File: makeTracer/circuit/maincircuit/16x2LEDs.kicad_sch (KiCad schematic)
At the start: 39 parts, among them P1 FrontsidePort, U2 74HC595, U3 74HC595

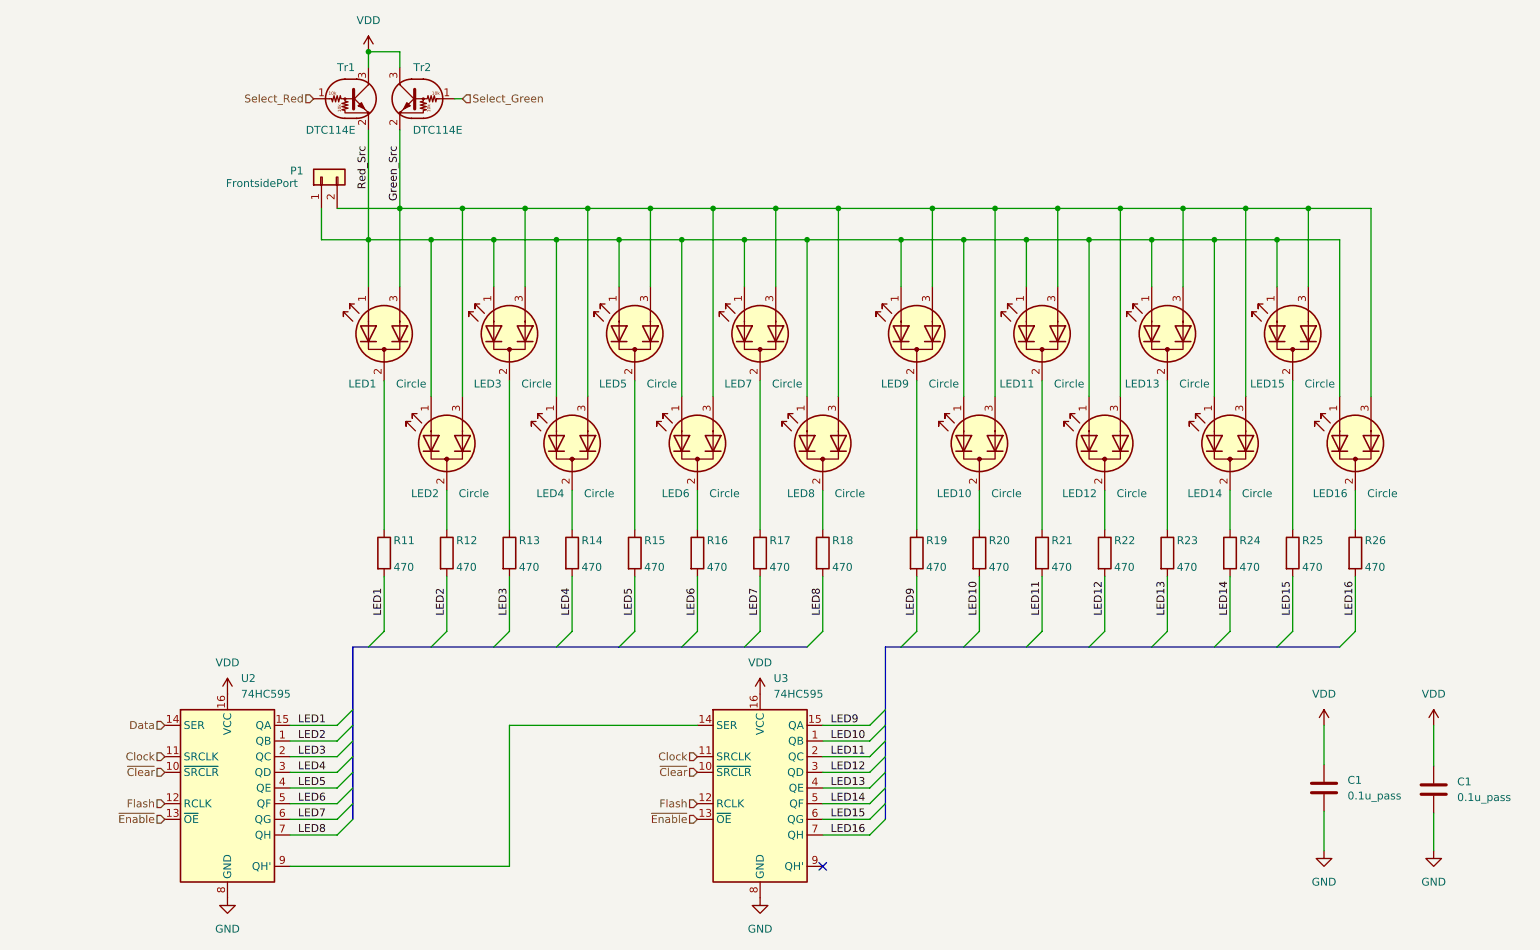
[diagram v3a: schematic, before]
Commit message: fix: .2mm to .4mm
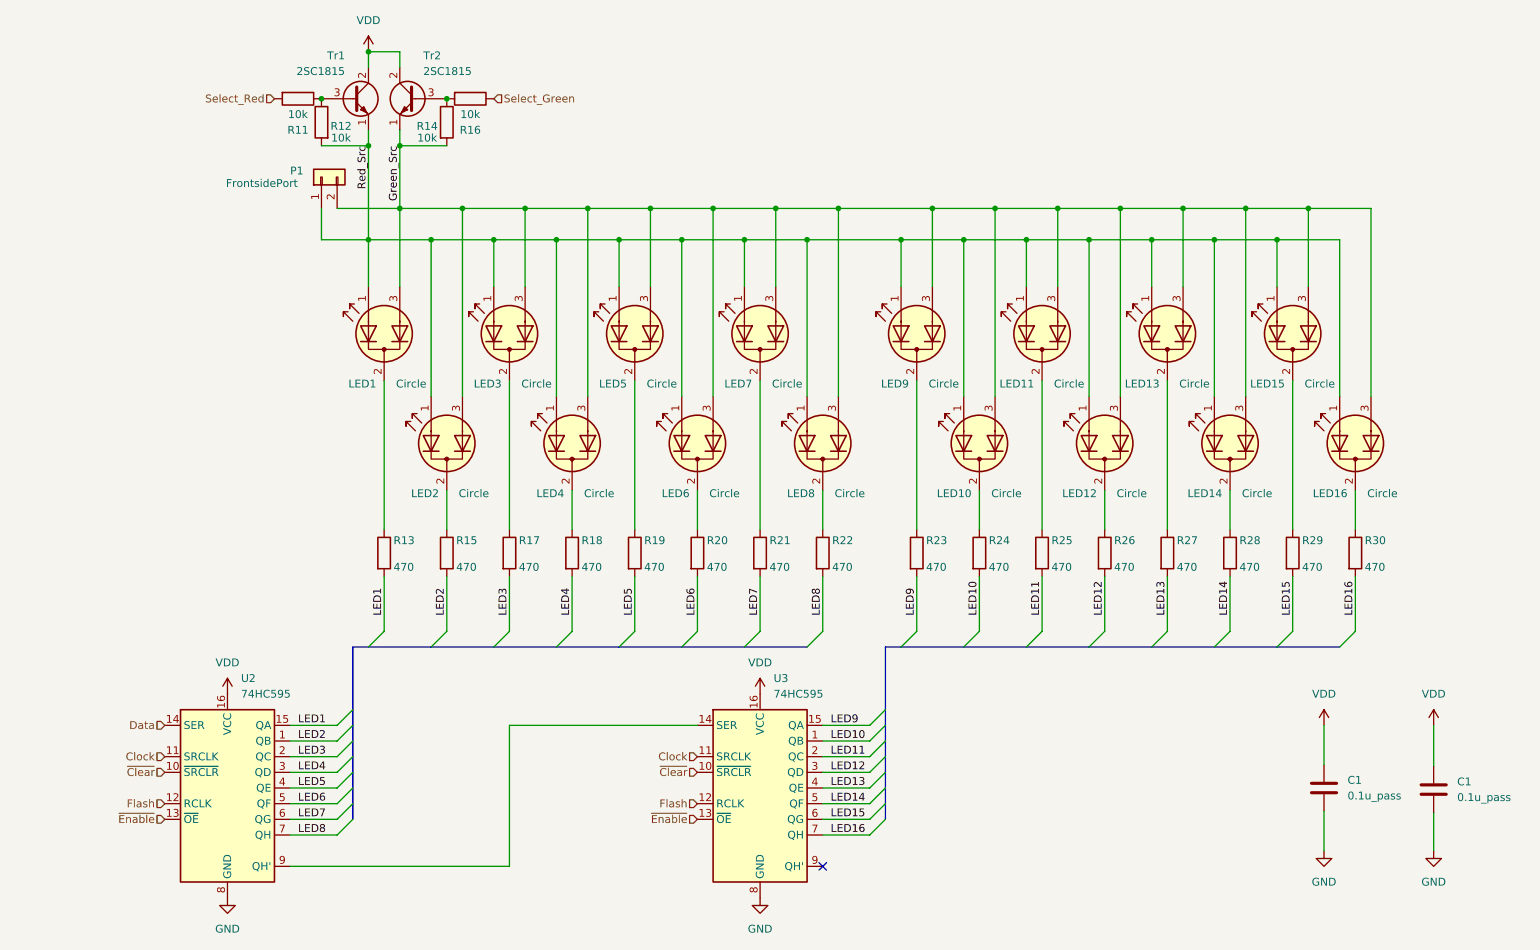
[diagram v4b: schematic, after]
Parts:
- removed Tr1, Tr2: DTC114E, Package_TO_SOT_THT:TO-92, symbol Transistor_BJT:DTC114E
- added R11, R14: 10k, Resistor_THT:R_Axial_DIN0207_L6.3mm_D2.5mm_P2.54mm_Vertical, symbol Device:R
- added R12, R16: 10k, Resistor_THT:R_Axial_DIN0207_L6.3mm_D2.5mm_P5.08mm_Vertical, symbol Device:R
- added Tr1, Tr2: 2SC1815, Package_TO_SOT_THT:TO-92_Inline_Wide, symbol Transistor_BJT:2SC1815
- R13: renamed from R11; footprint Resistor_THT:R_Axial_DIN0207_L6.3mm_D2.5mm_P7.62mm_Horizontal -> Resistor_THT:R_Axial_DIN0207_L6.3mm_D2.5mm_P10.16mm_Horizontal
- R18: renamed from R14; footprint Resistor_THT:R_Axial_DIN0207_L6.3mm_D2.5mm_P7.62mm_Horizontal -> Resistor_THT:R_Axial_DIN0207_L6.3mm_D2.5mm_P10.16mm_Horizontal
- R23: renamed from R19; footprint Resistor_THT:R_Axial_DIN0207_L6.3mm_D2.5mm_P7.62mm_Horizontal -> Resistor_THT:R_Axial_DIN0207_L6.3mm_D2.5mm_P10.16mm_Horizontal
- renumbered R12 to R15, R13 to R17, R15 to R19, R16 to R20, R17 to R21, R18 to R22, R20 to R24, R21 to R25, R22 to R26, R23 to R27, R24 to R28, R25 to R29, R26 to R30
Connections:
- net Green_Src: now also R14.2, Tr2.1 (E)
- net Red_Src: now also R12.2, Tr1.1 (E)
- net Select_Green: now also R16.1
- net Select_Red: now also R11.2
- net VDD: now also Tr1.2 (C), Tr2.2 (C)
- new net: R11.1, R12.1, Tr1.3 (B)
- new net: R14.1, R16.2, Tr2.3 (B)
